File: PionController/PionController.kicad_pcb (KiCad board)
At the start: 4 copper layers, 80 parts, among them J1 SM10B-ULHK-1TA1-ETB_HF_, J2 Conn_01x02, J3 Conn_01x02, J4 Conn_01x02, J6 Conn_01x02, J7 FTSH-107-01-L-DV-K-A, U1 STM32H743VITx, U2 TLV75733PDBV, U3 ISO1050DUB, U4 ISO1050DUB, U5 CA-IS3740HN, X1 ASE-16.00MHz, Y2 32.768kHZ

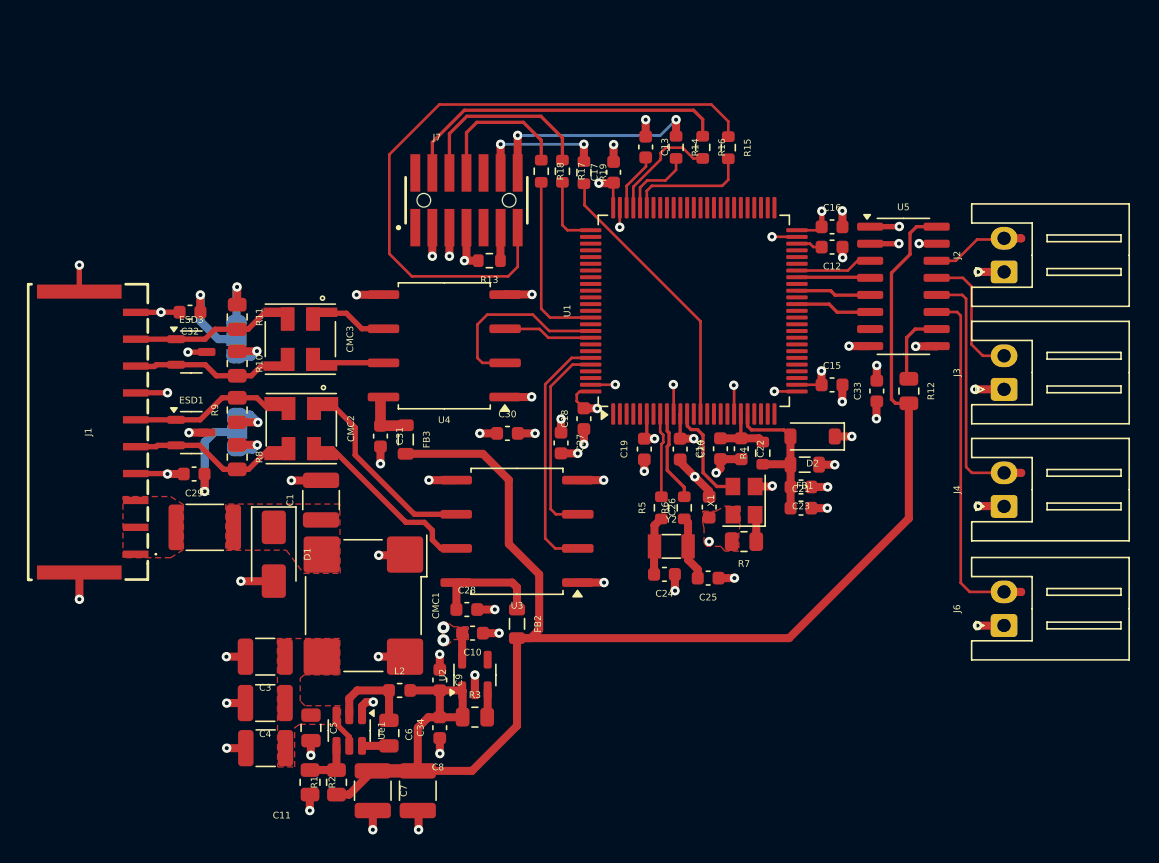
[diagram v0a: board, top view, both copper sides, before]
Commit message: adding board outline
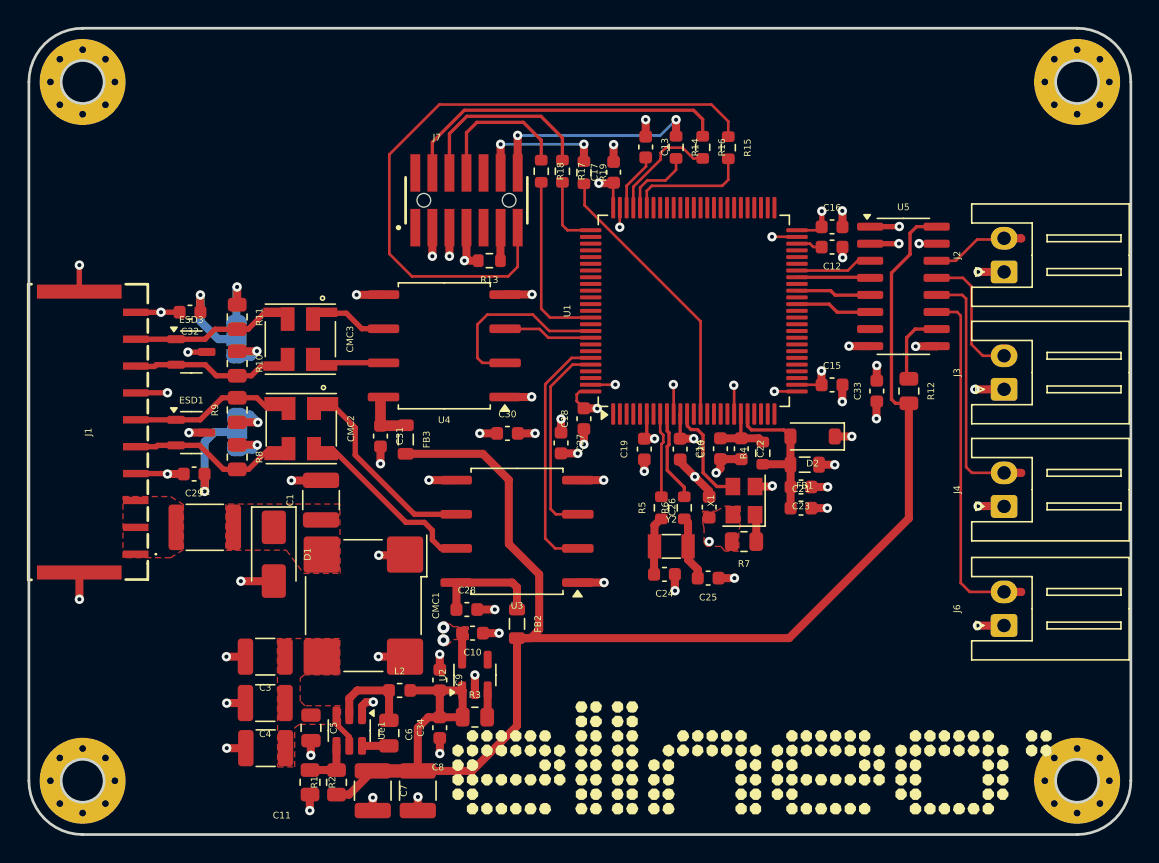
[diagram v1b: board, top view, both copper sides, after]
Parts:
- added H1: MountingHole_Pad, MountingHole:MountingHole_3.2mm_M3_Pad_Via, F.Cu at (104.0, 70.6)
- added H2: MountingHole_Pad, MountingHole:MountingHole_3.2mm_M3_Pad_Via, F.Cu at (178.0, 70.6)
- added H3: MountingHole_Pad, MountingHole:MountingHole_3.2mm_M3_Pad_Via, F.Cu at (178.0, 122.6)
- added H4: MountingHole_Pad, MountingHole:MountingHole_3.2mm_M3_Pad_Via, F.Cu at (104.0, 122.6)
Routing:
- net GND: track 106.3 -> 105.4 mm
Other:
- board outline added: 82 x 60 mm
- board text added: "PION"
- board text added: "V - 1.0"

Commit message: fixed Crystal osc and added a 5V and a 3.3V power plane
Added 5V and 3.3V power plane, fixed crystal oscylator, reordered some components
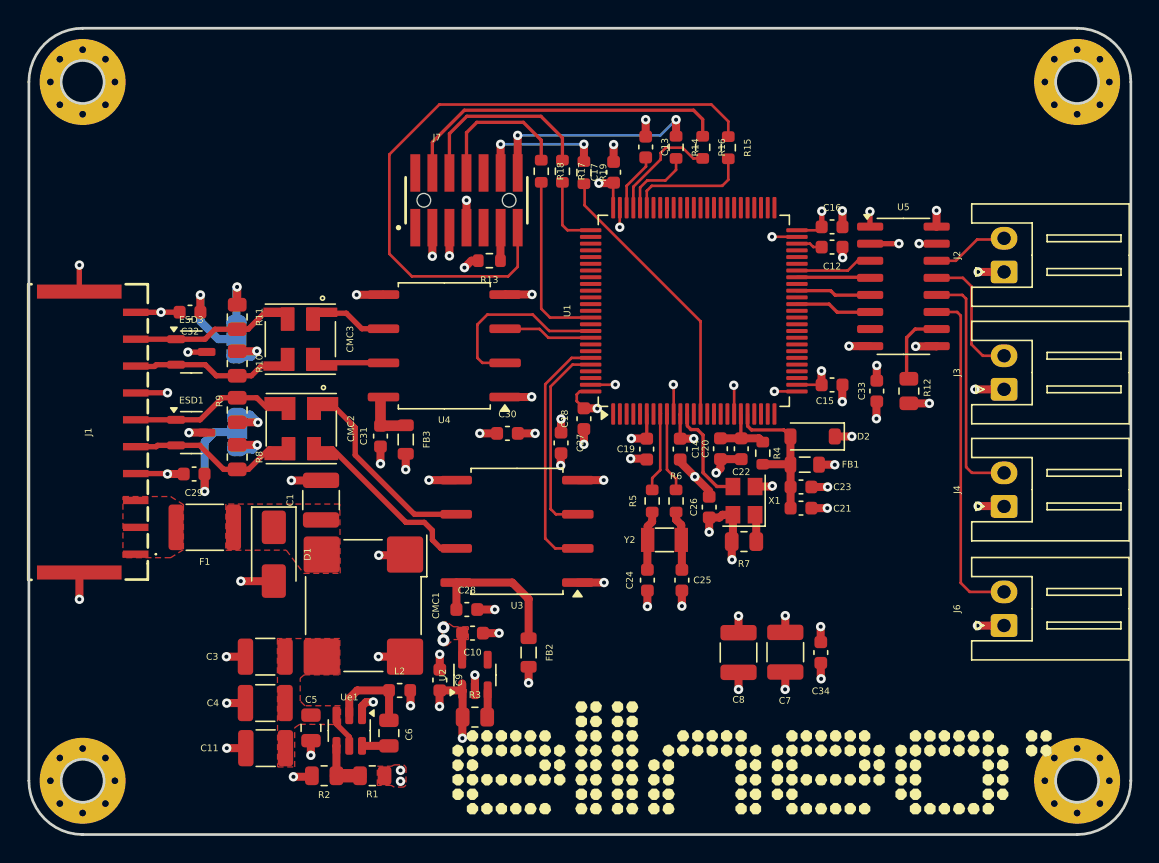
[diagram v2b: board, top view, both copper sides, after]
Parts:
- moved C7 32.4 mm to (156.3, 113.1), turned to 90 degrees
- moved C34 28.9 mm to (158.9, 113.1), turned to -90 degrees
- moved C8 26.0 mm to (152.8, 113.1), turned to 90 degrees
- moved R1 2.71 mm to (125.6, 122.3), turned to 180 degrees
- moved FB2 2.30 mm to (137.2, 113.1)
- moved C25 1.96 mm to (148.6, 107.7), turned to 90 degrees
- moved C24 1.34 mm to (146.0, 107.7), turned to 90 degrees
- moved R2 1.16 mm to (122.0, 122.3), turned to 180 degrees
- moved R5 0.85 mm to (146.4, 101.8)
- moved R6 0.79 mm to (148.2, 101.8)
- moved Y2 0.70 mm to (147.3, 104.7)
- moved C19 0.18 mm to (146.0, 98.0)
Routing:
- net +5V: track 117.5 -> 17.1 mm, vias 0 -> 12
- net +3.3V: track 34.2 -> 39.8 mm, vias 18 -> 19
- net Net-(U3-VCC2): track 8.34 -> 10.8 mm
- net Net-(J2-Pin_2): track 6.99 -> 5.59 mm
- net Net-(J6-Pin_2): track 26.6 -> 25.3 mm
- net Net-(J4-Pin_2): track 19.1 -> 17.8 mm
- net LSE_OSC_OUT: track 6.80 -> 5.96 mm
- net GND: track 105.4 -> 105.7 mm, vias 62 -> 63
- added copper zone on F.Cu, net +5V
- added copper zone on In2.Cu, net +5V

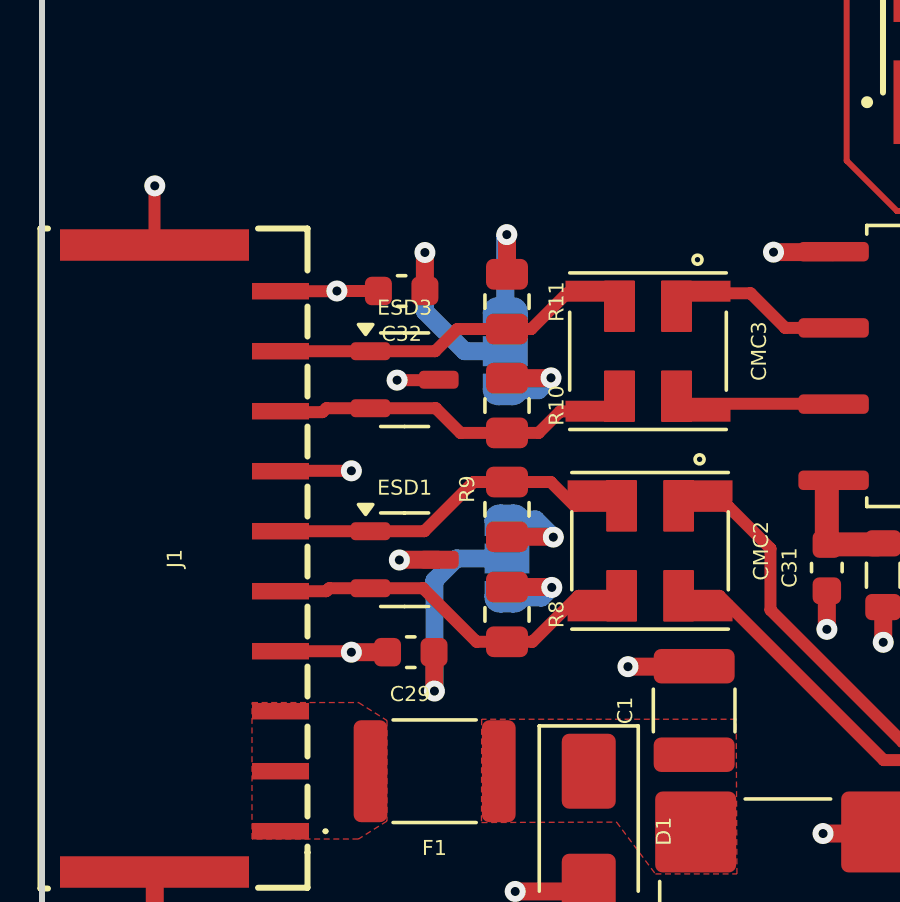
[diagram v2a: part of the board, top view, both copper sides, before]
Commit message: Can reorder
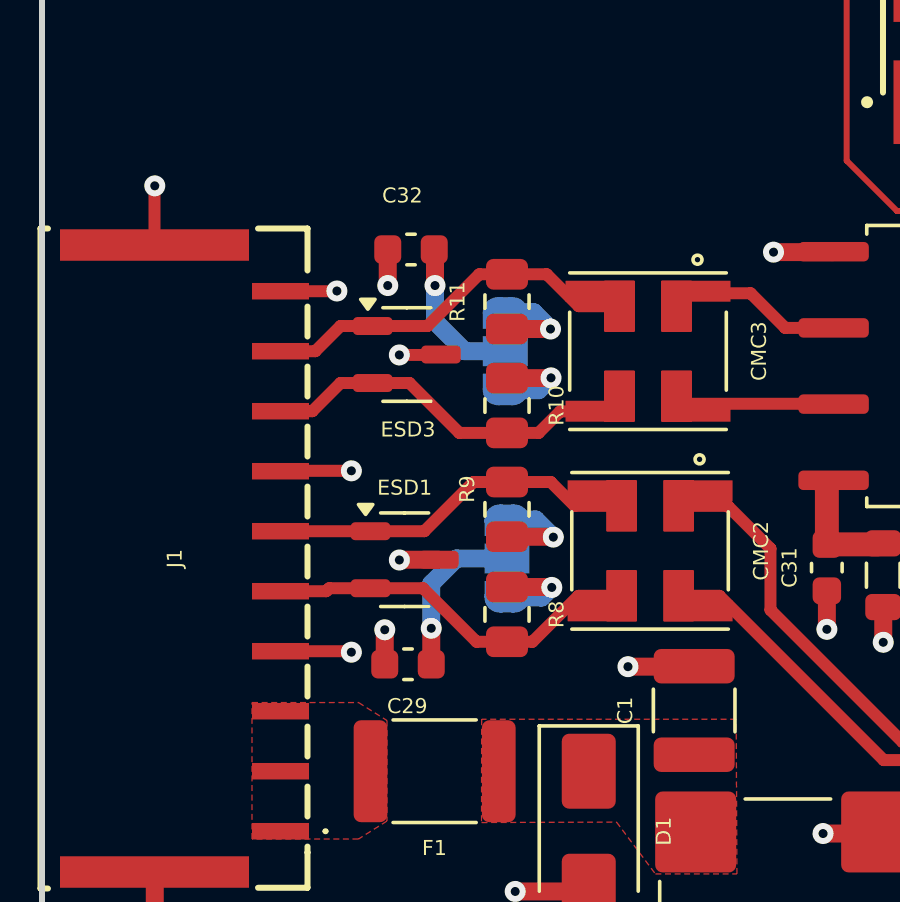
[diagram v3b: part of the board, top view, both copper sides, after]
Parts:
- moved C32 1.42 mm to (112.3, 86.4)
- moved ESD3 0.84 mm to (112.2, 89.9)
- moved C29 0.41 mm to (112.2, 100.2)
- turned R11 to 90 degrees
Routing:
- net Net-(SB1-C): track 7.71 -> 5.56 mm
- net Net-(SB2-C): track 6.47 -> 5.16 mm
- net CAN_COMM_L: track 12.3 -> 13.4 mm
- net Net-(SB2-B): track 3.93 -> 3.19 mm
- net CAN_COMM_H: track 12.2 -> 12.9 mm
- net GND: track 105.7 -> 105.5 mm, vias 63 -> 65

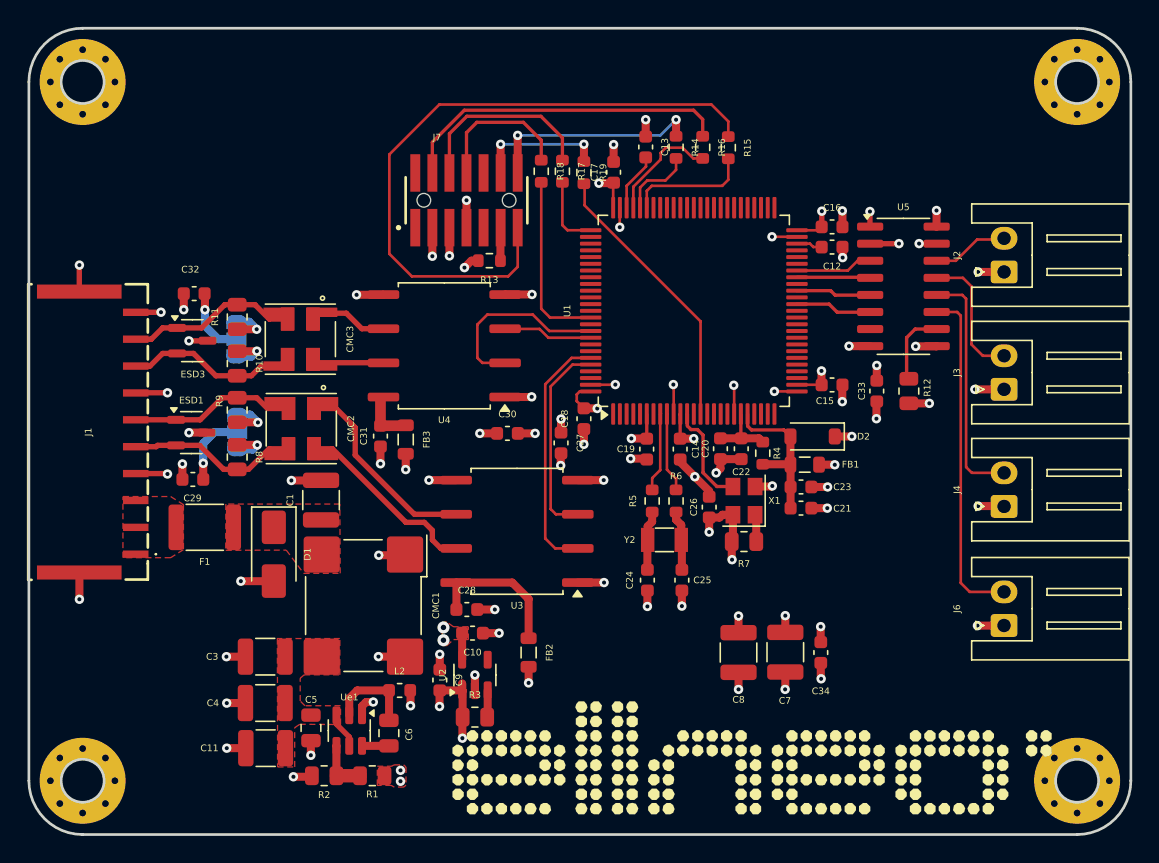
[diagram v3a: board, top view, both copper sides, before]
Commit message: Fixing issues with decoupling capacitors and addressing other minor adjustments.
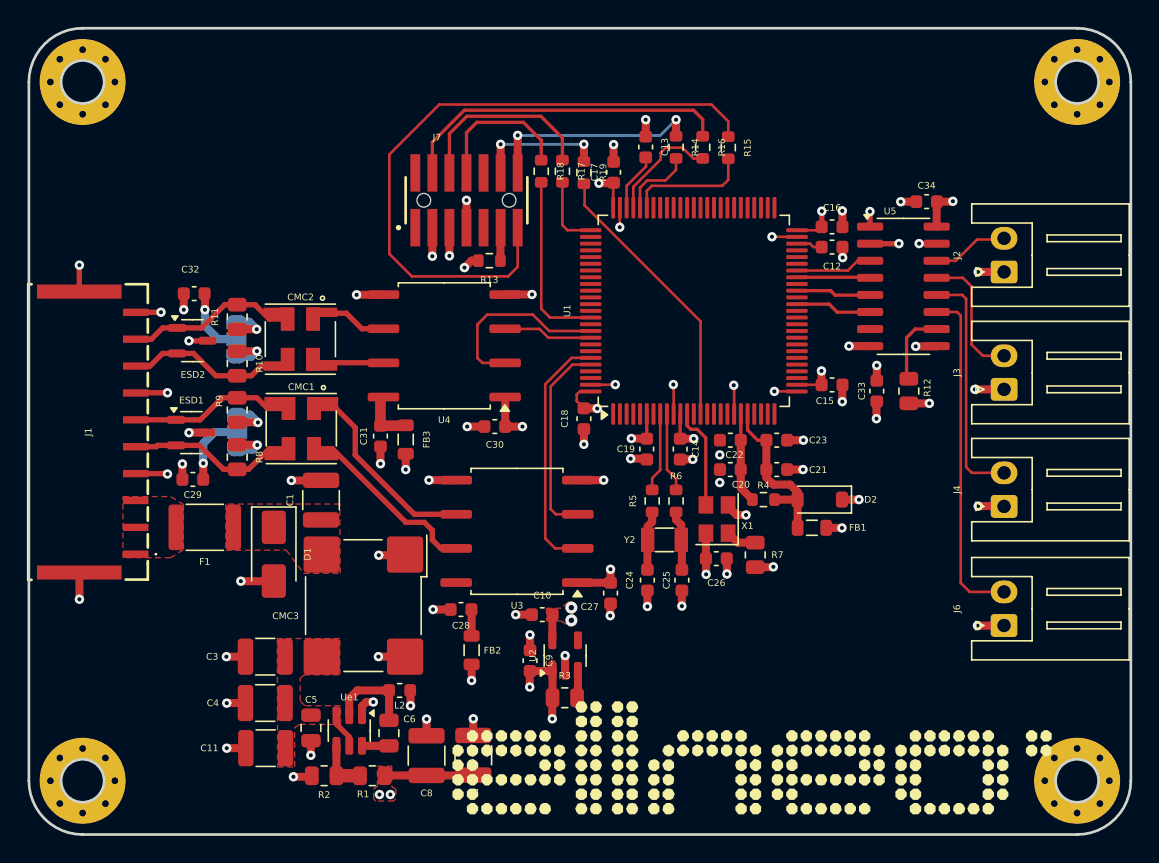
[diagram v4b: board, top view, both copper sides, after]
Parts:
- moved C34 34.5 mm to (166.8, 79.6), turned to 0 degrees
- moved C7 24.5 mm to (133.1, 120.8)
- moved C8 24.5 mm to (129.6, 120.8)
- moved C27 11.8 mm to (143.3, 108.7)
- moved C9 6.87 mm to (137.3, 113.7)
- moved U2 6.87 mm to (139.9, 113.3)
- moved R3 6.84 mm to (139.9, 116.5)
- moved C10 5.37 mm to (138.2, 110.3), turned to 0 degrees
- moved D2 4.73 mm to (158.9, 101.7)
- moved FB1 4.73 mm to (158.3, 103.8)
- moved FB2 4.25 mm to (132.9, 112.9)
- moved C23 3.92 mm to (155.7, 97.3)
- moved C26 3.87 mm to (151.2, 106.1), turned to 180 degrees
- moved R4 3.45 mm to (154.7, 101.7), turned to 180 degrees
- moved C21 3.39 mm to (155.7, 99.5)
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- renumbered CMC2 to CMC1, CMC3 to CMC2, CMC1 to CMC3, ESD3 to ESD2
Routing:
- net Net-(U3-VCC2): track 10.8 -> 1.99 mm
- net +5V: track 17.1 -> 21.9 mm, vias 12 -> 9
- net GND: track 105.5 -> 101.6 mm, vias 65 -> 67
- net VREF: track 5.14 -> 6.73 mm
- net VDDA: track 11.8 -> 13.2 mm
- net +3.3V: track 39.8 -> 38.7 mm, vias 19 -> 17
